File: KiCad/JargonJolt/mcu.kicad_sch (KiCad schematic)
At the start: 19 parts, among them J1 Conn_01x05, Q1 SS8050-G, Q2 SS8050-G, SW1 SW_Push, SW2 SW_Push, U1 ESP32-S3-WROOM-1-N16R2

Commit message: worked on pinout
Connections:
- net SCL: now reaches U1.10 (IO17)
- net SDA: now reaches U1.11 (IO18)
- net MCLK: now reaches U1.13 (IO19)
- net BCLK: now reaches U1.14 (IO20)
- net HSPI_SCLK: now reaches U1.18 (IO10)
- net HSPI_MISO: now reaches U1.19 (IO11)
- net HSPI_MOSI: now reaches U1.20 (IO12)
- net HSPI_CS1: now reaches U1.21 (IO13)
- net HSPI_CS2: now reaches U1.22 (IO14)
- net WS: now reaches U1.23 (IO21)
- net DIN/DOUT: now reaches U1.28 (IO35)
- net VSPI_SCLK: now reaches U1.31 (IO38)
- net VSPI_MISO: now reaches U1.32 (IO39)
- net VSPI_MOSI: now reaches U1.33 (IO40)
- net VSPI_CS1: now reaches U1.34 (IO41)
- net VSPI_CS2: now reaches U1.35 (IO42)
- net SPI01_DATA: now reaches U1.39 (IO1)
- net BUTTON1: now reaches U1.4 (IO4)
- net BUTTON2: now reaches U1.5 (IO5)
- net BUTTON3: now reaches U1.6 (IO6)
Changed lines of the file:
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@@
     (stroke (width 0) (type default))
   )
-  (polyline (pts (xy 12.065 139.065) (xy 123.825 139.065))
+  (polyline (pts (xy 12.319 167.513) (xy 124.333 167.767))
     (stroke (width 0) (type dash))
   )
@@
     (stroke (width 0) (type default))
   )
-  (polyline (pts (xy 123.825 90.17) (xy 123.825 139.065))
+  (polyline (pts (xy 123.825 90.17) (xy 124.333 167.767))
     (stroke (width 0) (type dash))
   )
@@
     (effects (font (size 1.27 1.27)) (justify left bottom))
   )
+  (label "HSPI_MISO" (at 172.085 98.425 180) (fields_autoplaced)
+    (effects (font (size 1.27 1.27)) (justify right bottom))
+  )
   (label "DTR" (at 67.945 106.68 180) (fields_autoplaced)
     (effects (font (size 1.27 1.27)) (justify right bottom))
   )
+  (label "SPI01_DATA" (at 172.085 73.025 180) (fields_autoplaced)
+    (effects (font (size 1.27 1.27)) (justify right bottom))
+  )
   (label "RTS" (at 68.58 121.92 180) (fields_autoplaced)
     (effects (font (size 1.27 1.27)) (justify right bottom))
@@
     (effects (font (size 1.27 1.27)) (justify right bottom))
   )
+  (label "DIN{slash}DOUT" (at 202.565 83.185 0) (fields_autoplaced)
+    (effects (font (size 1.27 1.27)) (justify left bottom))
+  )
+  (label "SDA" (at 202.565 73.025 0) (fields_autoplaced)
+    (effects (font (size 1.27 1.27)) (justify left bottom))
+  )
+  (label "HSPI_CS1" (at 172.085 103.505 180) (fields_autoplaced)
+    (effects (font (size 1.27 1.27)) (justify right bottom))
+  )
   (label "GPIO45_STRAP" (at 202.565 103.505 0) (fields_autoplaced)
     (effects (font (size 1.27 1.27)) (justify left bottom))
@@
     (effects (font (size 1.27 1.27)) (justify left bottom))
   )
+  (label "HSPI_CS2" (at 172.085 106.045 180) (fields_autoplaced)
+    (effects (font (size 1.27 1.27)) (justify right bottom))
+  )
+  (label "HSPI_MOSI" (at 172.085 100.965 180) (fields_autoplaced)
+    (effects (font (size 1.27 1.27)) (justify right bottom))
+  )
+  (label "HSPI_SCLK" (at 172.085 95.885 180) (fields_autoplaced)
+    (effects (font (size 1.27 1.27)) (justify right bottom))
+  )
   (label "Rx" (at 36.195 118.11 0) (fields_autoplaced)
     (effects (font (size 1.27 1.27)) (justify left bottom))
   )
+  (label "SCL" (at 202.565 70.485 0) (fields_autoplaced)
+    (effects (font (size 1.27 1.27)) (justify left bottom))
+  )
+  (label "WS" (at 202.565 80.645 0) (fields_autoplaced)
+    (effects (font (size 1.27 1.27)) (justify left bottom))
+  )
   (label "CHIP_PU" (at 41.275 37.465 180) (fields_autoplaced)
     (effects (font (size 1.27 1.27)) (justify right bottom))
@@
     (effects (font (size 1.27 1.27)) (justify right bottom))
   )
+  (label "MCLK" (at 202.565 75.565 0) (fields_autoplaced)
+    (effects (font (size 1.27 1.27)) (justify left bottom))
+  )
+  (label "BCLK" (at 202.565 78.105 0) (fields_autoplaced)
+    (effects (font (size 1.27 1.27)) (justify left bottom))
+  )
   (label "GPIO3_STRAP" (at 172.085 78.105 180) (fields_autoplaced)
     (effects (font (size 1.27 1.27)) (justify right bottom))
   )
+  (hierarchical_label "VSPI_CS1" (shape input) (at 202.565 98.425 0) (fields_autoplaced)
+    (effects (font (size 1.27 1.27)) (justify left))
+  )
+  (hierarchical_label "VSPI_MISO" (shape input) (at 202.565 93.345 0) (fields_autoplaced)
+    (effects (font (size 1.27 1.27)) (justify left))
+  )
+  (hierarchical_label "VSPI_MOSI" (shape input) (at 202.565 95.885 0) (fields_autoplaced)
+    (effects (font (size 1.27 1.27)) (justify left))
+  )
+  (hierarchical_label "BUTTON2" (shape input) (at 172.085 83.185 180) (fields_autoplaced)
+    (effects (font (size 1.27 1.27)) (justify right))
+  )
+  (hierarchical_label "BUTTON3" (shape input) (at 172.085 85.725 180) (fields_autoplaced)
+    (effects (font (size 1.27 1.27)) (justify right))
+  )
+  (hierarchical_label "VSPI_SCLK" (shape input) (at 202.565 90.805 0) (fields_autoplaced)
+    (effects (font (size 1.27 1.27)) (justify left))
+  )
+  (hierarchical_label "VSPI_CS2" (shape input) (at 202.565 100.965 0) (fields_autoplaced)
+    (effects (font (size 1.27 1.27)) (justify left))
+  )
+  (hierarchical_label "BUTTON1" (shape input) (at 172.085 80.645 180) (fields_autoplaced)
+    (effects (font (size 1.27 1.27)) (justify right))
+  )
   (symbol (lib_id "Device:R") (at 86.36 42.545 270) (unit 1)

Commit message: worked on schematic
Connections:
- net +3V3 renamed +3.3VA
- net SPI01_DATA: no longer names the net of U1.39 (IO1)

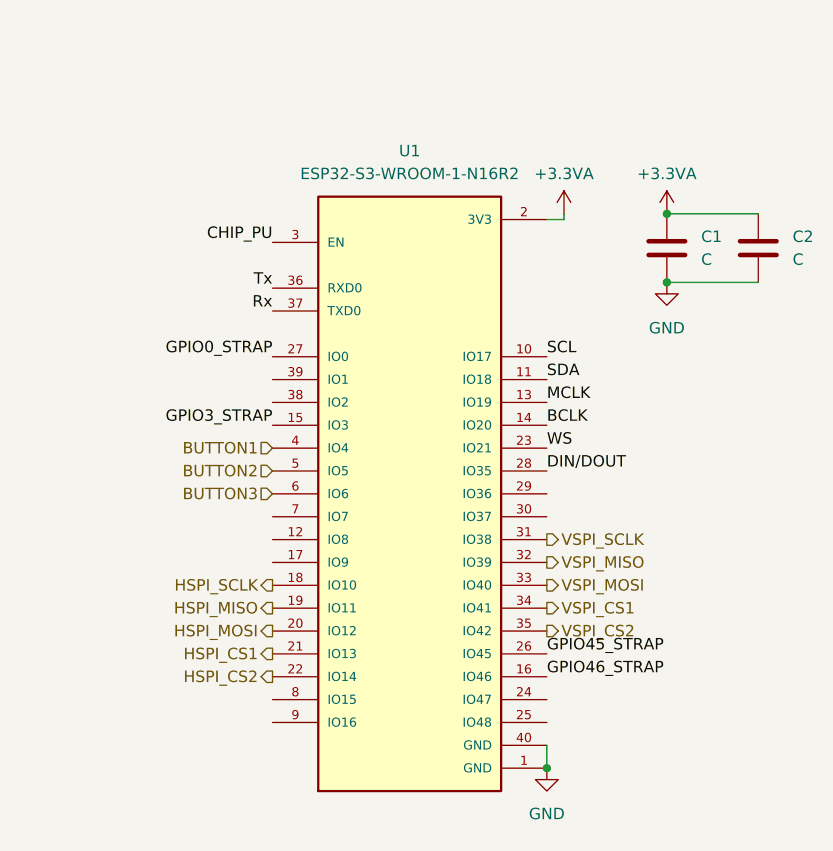
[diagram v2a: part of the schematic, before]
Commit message: added i2s schematic
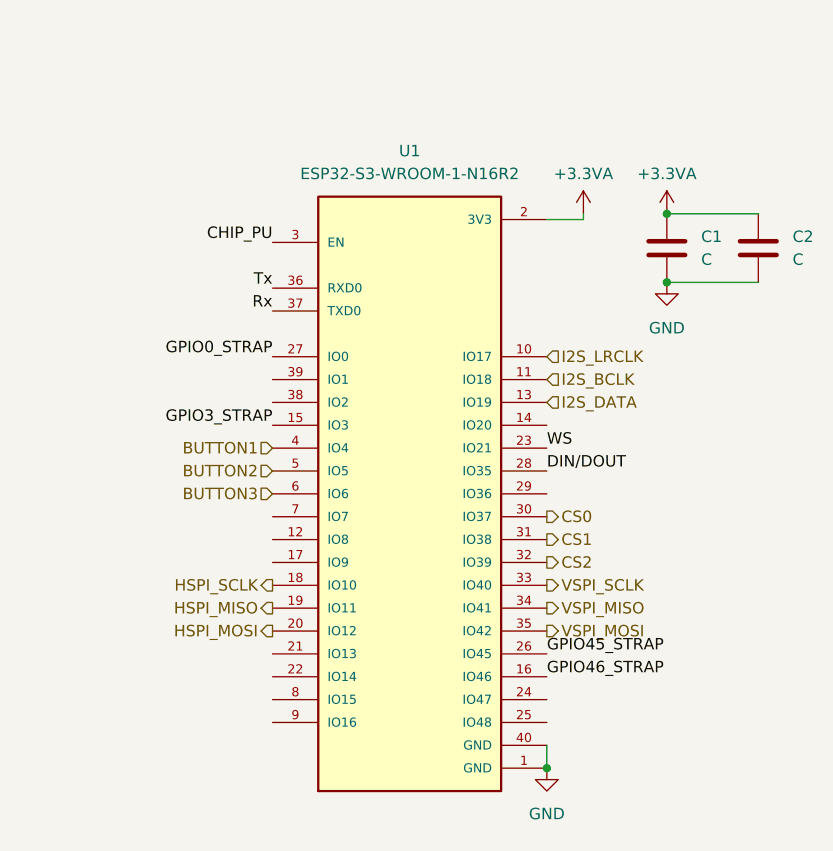
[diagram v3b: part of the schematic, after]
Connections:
- net VSPI_CS1 is gone; now on net VSPI_MISO: U1.34 (IO41)
- net VSPI_CS2 is gone; now on net VSPI_MOSI: U1.35 (IO42)
- net VSPI_MISO: no longer U1.32 (IO39)
- net VSPI_MOSI: no longer U1.33 (IO40)
- net VSPI_SCLK: now also U1.33 (IO40); no longer U1.31 (IO38)
- net CS0: now reaches U1.30 (IO37)
- net BCLK: no longer names the net of U1.14 (IO20)
- net HSPI_CS1: no longer names the net of U1.21 (IO13)
- net HSPI_CS2: no longer names the net of U1.22 (IO14)
- net MCLK renamed I2S_DATA
- net SCL renamed I2S_LRCLK
- net SDA renamed I2S_BCLK
- new net CS1: U1.31 (IO38)
- new net CS2: U1.32 (IO39)
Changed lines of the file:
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@@
     (stroke (width 0) (type default))
   )
-  (wire (pts (xy 204.47 54.61) (xy 204.47 55.245))
+  (wire (pts (xy 206.629 54.61) (xy 206.629 55.245))
     (stroke (width 0) (type default))
   )
@@
     (stroke (width 0) (type default))
   )
-  (wire (pts (xy 204.47 55.245) (xy 202.565 55.245))
+  (wire (pts (xy 206.629 55.245) (xy 202.565 55.245))
     (stroke (width 0) (type default))
   )
@@
     (effects (font (size 1.27 1.27)) (justify left bottom))
   )
-  (label "SDA" (at 202.565 73.025 0) (fields_autoplaced)
-    (effects (font (size 1.27 1.27)) (justify left bottom))
-  )
   (label "GPIO45_STRAP" (at 202.565 103.505 0) (fields_autoplaced)
     (effects (font (size 1.27 1.27)) (justify left bottom))
@@
     (effects (font (size 1.27 1.27)) (justify left bottom))
   )
-  (label "SCL" (at 202.565 70.485 0) (fields_autoplaced)
-    (effects (font (size 1.27 1.27)) (justify left bottom))
-  )
   (label "WS" (at 202.565 80.645 0) (fields_autoplaced)
     (effects (font (size 1.27 1.27)) (justify left bottom))
@@
     (effects (font (size 1.27 1.27)) (justify right bottom))
   )
-  (label "MCLK" (at 202.565 75.565 0) (fields_autoplaced)
-    (effects (font (size 1.27 1.27)) (justify left bottom))
-  )
-  (label "BCLK" (at 202.565 78.105 0) (fields_autoplaced)
-    (effects (font (size 1.27 1.27)) (justify left bottom))
-  )
   (label "GPIO3_STRAP" (at 172.085 78.105 180) (fields_autoplaced)
     (effects (font (size 1.27 1.27)) (justify right bottom))
   )
-  (hierarchical_label "VSPI_CS1" (shape output) (at 202.565 98.425 0) (fields_autoplaced)
-    (effects (font (size 1.27 1.27)) (justify left))
-  )
   (hierarchical_label "HSPI_MOSI" (shape output) (at 172.085 100.965 180) (fields_autoplaced)
     (effects (font (size 1.27 1.27)) (justify right))
   )
-  (hierarchical_label "VSPI_MISO" (shape output) (at 202.565 93.345 0) (fields_autoplaced)
+  (hierarchical_label "VSPI_MISO" (shape output) (at 202.565 98.425 0) (fields_autoplaced)
     (effects (font (size 1.27 1.27)) (justify left))
   )
@@
     (effects (font (size 1.27 1.27)) (justify right))
   )
-  (hierarchical_label "VSPI_MOSI" (shape output) (at 202.565 95.885 0) (fields_autoplaced)
-    (effects (font (size 1.27 1.27)) (justify left))
-  )
-  (hierarchical_label "HSPI_CS1" (shape output) (at 172.085 103.505 180) (fields_autoplaced)
-    (effects (font (size 1.27 1.27)) (justify right))
+  (hierarchical_label "VSPI_MOSI" (shape output) (at 202.565 100.965 0) (fields_autoplaced)
+    (effects (font (size 1.27 1.27)) (justify left))
+  )
+  (hierarchical_label "I2S_BCLK" (shape input) (at 202.565 73.025 0) (fields_autoplaced)
+    (effects (font (size 1.27 1.27)) (justify left))
   )
   (hierarchical_label "HSPI_MISO" (shape output) (at 172.085 98.425 180) (fields_autoplaced)
     (effects (font (size 1.27 1.27)) (justify right))
   )
-  (hierarchical_label "HSPI_CS2" (shape output) (at 172.085 106.045 180) (fields_autoplaced)
-    (effects (font (size 1.27 1.27)) (justify right))
+  (hierarchical_label "I2S_LRCLK" (shape input) (at 202.565 70.485 0) (fields_autoplaced)
+    (effects (font (size 1.27 1.27)) (justify left))
+  )
+  (hierarchical_label "CS0" (shape output) (at 202.565 88.265 0) (fields_autoplaced)
+    (effects (font (size 1.27 1.27)) (justify left))
   )
   (hierarchical_label "BUTTON2" (shape input) (at 172.085 83.185 180) (fields_autoplaced)
     (effects (font (size 1.27 1.27)) (justify right))
   )
+  (hierarchical_label "I2S_DATA" (shape input) (at 202.565 75.565 0) (fields_autoplaced)
+    (effects (font (size 1.27 1.27)) (justify left))
+  )
   (hierarchical_label "BUTTON3" (shape input) (at 172.085 85.725 180) (fields_autoplaced)
     (effects (font (size 1.27 1.27)) (justify right))
   )
-  (hierarchical_label "VSPI_SCLK" (shape output) (at 202.565 90.805 0) (fields_autoplaced)
-    (effects (font (size 1.27 1.27)) (justify left))
-  )
-  (hierarchical_label "VSPI_CS2" (shape output) (at 202.565 100.965 0) (fields_autoplaced)
+  (hierarchical_label "VSPI_SCLK" (shape output) (at 202.565 95.885 0) (fields_autoplaced)
     (effects (font (size 1.27 1.27)) (justify left))
   )
   (hierarchical_label "BUTTON1" (shape input) (at 172.085 80.645 180) (fields_autoplaced)
     (effects (font (size 1.27 1.27)) (justify right))
+  )
+  (hierarchical_label "CS1" (shape output) (at 202.565 90.805 0) (fields_autoplaced)
+    (effects (font (size 1.27 1.27)) (justify left))
+  )
+  (hierarchical_label "CS2" (shape output) (at 202.565 93.345 0) (fields_autoplaced)
+    (effects (font (size 1.27 1.27)) (justify left))
   )
   (symbol (lib_id "Device:R") (at 86.36 42.545 270) (unit 1)
@@
     )
   )
-  (symbol (lib_id "power:+3.3VA") (at 204.47 54.61 0) (unit 1)
+  (symbol (lib_id "power:+3.3VA") (at 206.629 54.61 0) (unit 1)
     (in_bom yes) (on_board yes) (dnp no) (fields_autoplaced)
-    (property "Reference" "#PWR02" (at 204.47 58.42 0)
-      (effects (font (size 1.27 1.27)) hide)
-    )
-    (property "Value" "+3.3VA" (at 204.47 50.165 0)
+    (property "Reference" "#PWR02" (at 206.629 58.42 0)
+      (effects (font (size 1.27 1.27)) hide)
+    )
+    (property "Value" "+3.3VA" (at 206.629 50.165 0)
       (effects (font (size 1.27 1.27)))
     )
-    (property "Footprint" "" (at 204.47 54.61 0)
-      (effects (font (size 1.27 1.27)) hide)
-    )
-    (property "Datasheet" "" (at 204.47 54.61 0)
-      (effects (font (size 1.27 1.27)) hide)
-    )
+    (property "Footprint" "" (at 206.629 54.61 0)
+      (effects (font (size 1.27 1.27)) hide)
+    )
+    (property "Datasheet" "" (at 206.629 54.61 0)
+      (effects (font (size 1.27 1.27)) hide)
+    )

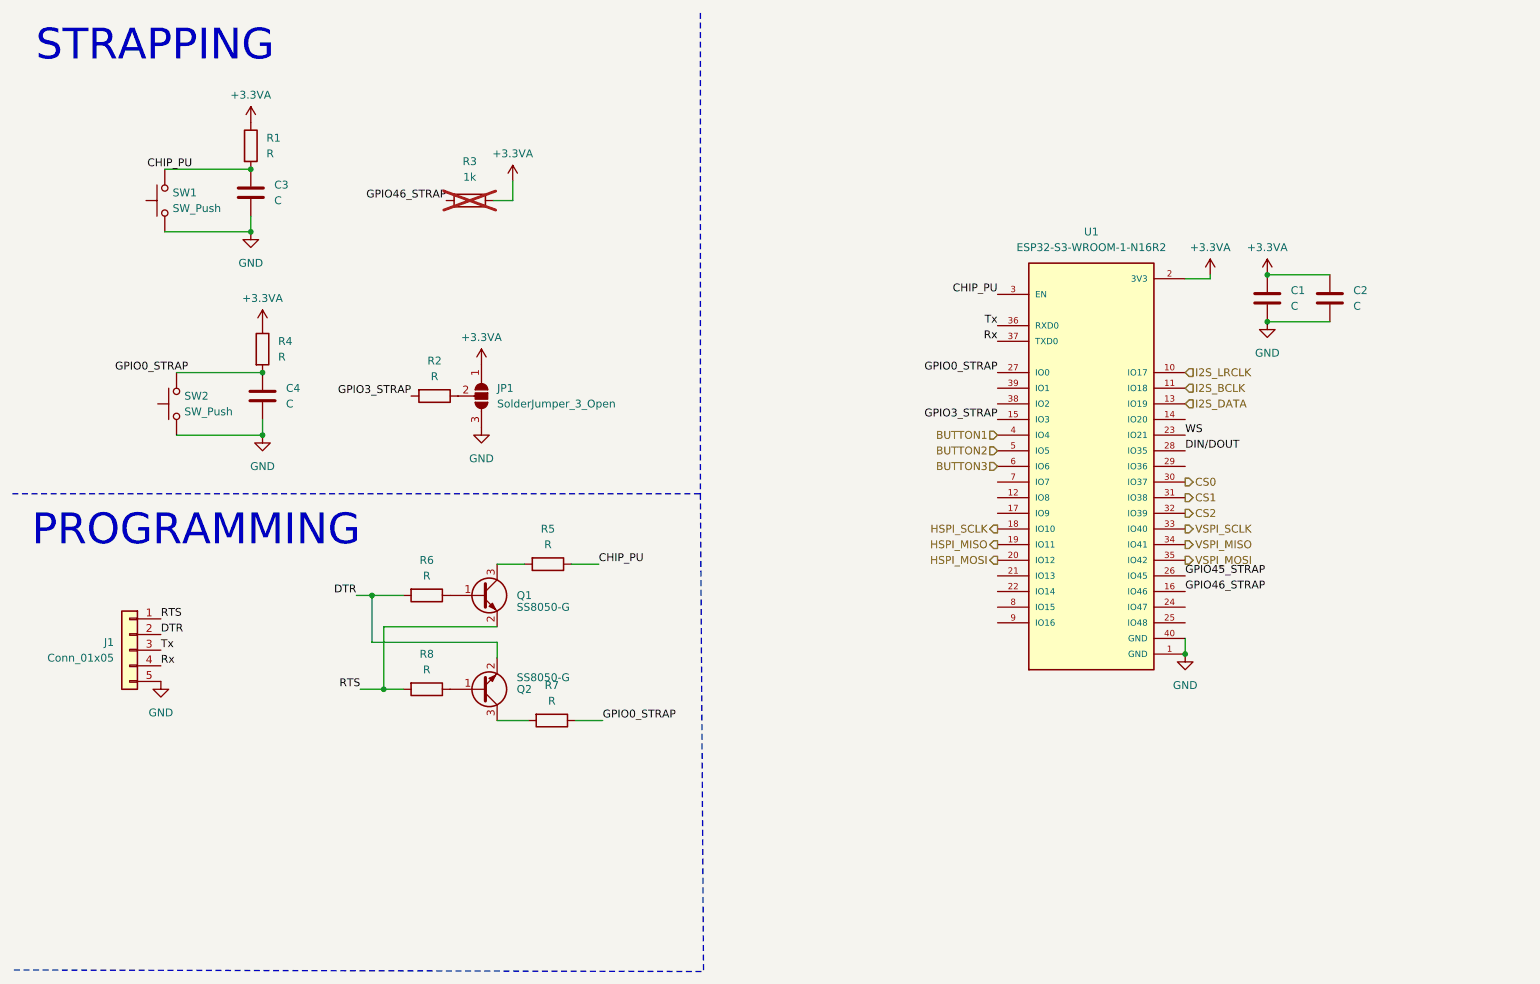
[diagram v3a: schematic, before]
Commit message: added sd module + fixed CS pins
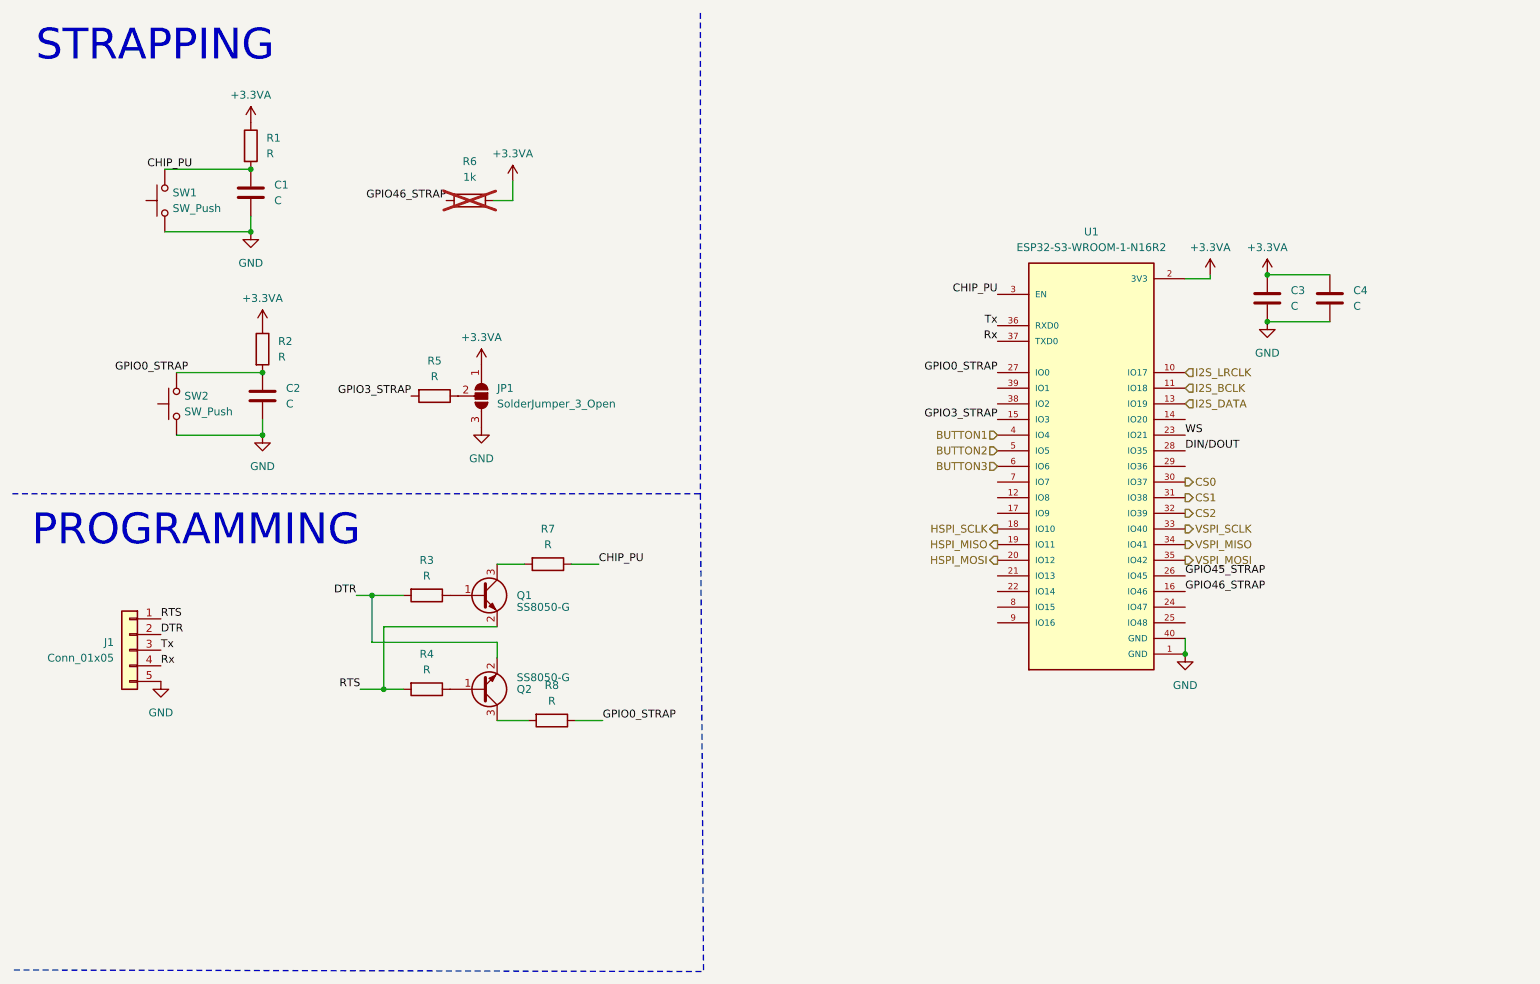
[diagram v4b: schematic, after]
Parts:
- renumbered C3 to C1, C4 to C2, C1 to C3, C2 to C4, R4 to R2, R6 to R3, R8 to R4, R2 to R5, R3 to R6, R5 to R7, R7 to R8
